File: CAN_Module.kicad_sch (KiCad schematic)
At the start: 14 parts, among them U3 SN65HVD231

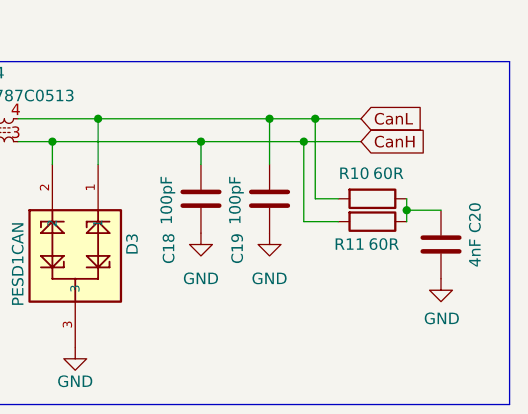
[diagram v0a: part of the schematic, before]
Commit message: added psu and formated board outline
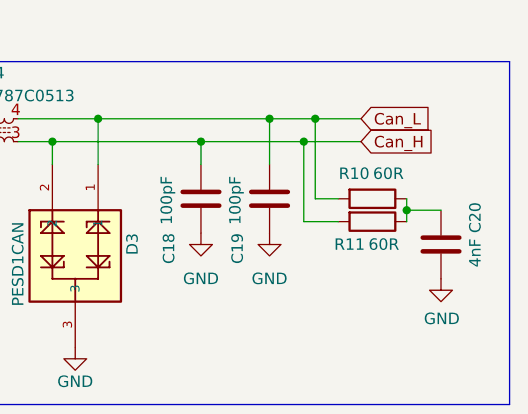
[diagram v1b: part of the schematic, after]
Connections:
- net CanH renamed Can_H
- net CanL renamed Can_L
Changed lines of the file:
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@@
 		)
 	)
-	(global_label "CanH"
+	(global_label "Can_H"
 		(shape input)
 		(at 144.78 26.67 0)
@@
 		)
 		(property "Intersheetrefs" "${INTERSHEET_REFS}"
-			(at 152.6637 26.67 0)
+			(at 153.6313 26.67 0)
 			(effects
 				(font
@@
 		)
 	)
-	(global_label "CanL"
+	(global_label "Can_L"
 		(shape input)
 		(at 144.78 24.13 0)
@@
 		)
 		(property "Intersheetrefs" "${INTERSHEET_REFS}"
-			(at 152.3613 24.13 0)
+			(at 153.3289 24.13 0)
 			(effects
 				(font

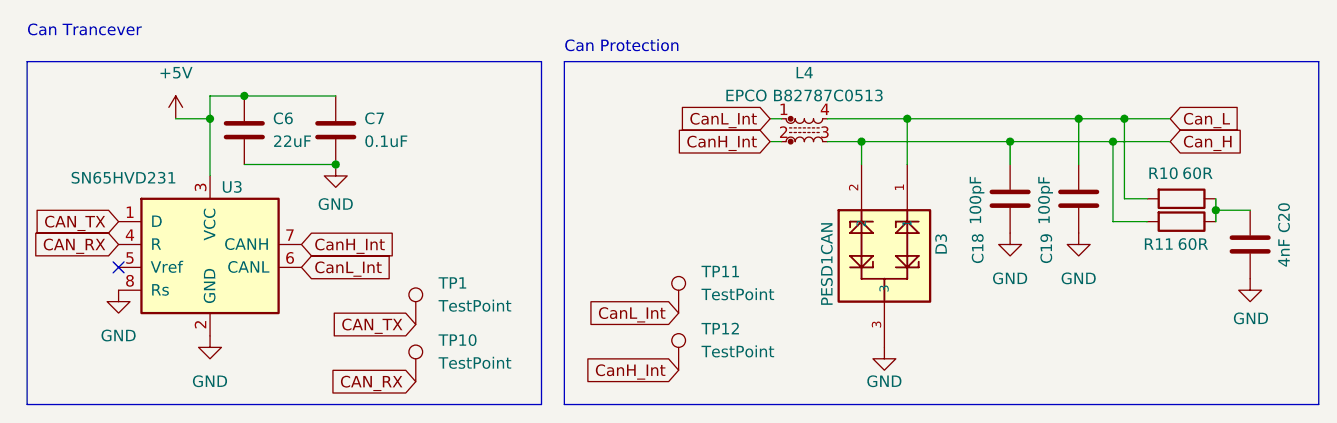
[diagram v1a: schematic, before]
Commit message: added footprint for a7670e
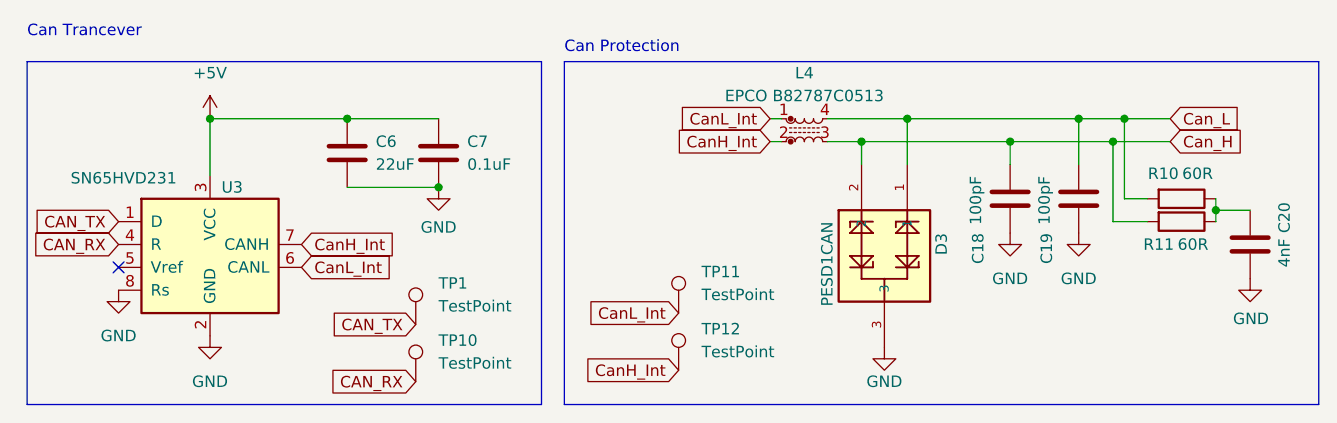
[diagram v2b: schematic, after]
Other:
- moved on the sheet: C6, C7
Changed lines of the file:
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@@
+	)
+	(junction
+		(at 134.62 24.13)
+		(diameter 0)
+		(color 0 0 0 0)
+	)
+	(junction
+		(at 127 26.67)
+		(diameter 0)
+		(color 0 0 0 0)
+	)
+	(junction
+		(at 115.57 24.13)
+		(diameter 0)
+		(color 0 0 0 0)
+	)
+	(junction
+		(at 149.86 34.29)
+		(diameter 0)
+		(color 0 0 0 0)
+	)
+	(junction
+		(at 110.49 26.67)
+		(diameter 0)
+		(color 0 0 0 0)
+	)
+	(junction
+		(at 138.43 26.67)
+		(diameter 0)
+		(color 0 0 0 0)
+	)
+	(junction
+		(at 53.34 24.13)
+		(diameter 0)
+		(color 0 0 0 0)
+	)
+	(junction
+		(at 63.5 31.75)
+		(diameter 0)
+		(color 0 0 0 0)
 	)
 	(junction
@@
 		(color 0 0 0 0)
 	)
-	(junction
-		(at 134.62 24.13)
-		(diameter 0)
-		(color 0 0 0 0)
-	)
-	(junction
-		(at 127 26.67)
-		(diameter 0)
-		(color 0 0 0 0)
-	)
-	(junction
-		(at 115.57 24.13)
-		(diameter 0)
-		(color 0 0 0 0)
-	)
-	(junction
-		(at 149.86 34.29)
-		(diameter 0)
-		(color 0 0 0 0)
-	)
-	(junction
-		(at 41.91 21.59)
-		(diameter 0)
-		(color 0 0 0 0)
-	)
-	(junction
-		(at 110.49 26.67)
-		(diameter 0)
-		(color 0 0 0 0)
-	)
-	(junction
-		(at 138.43 26.67)
-		(diameter 0)
-		(color 0 0 0 0)
-	)
-	(junction
-		(at 52.07 29.21)
-		(diameter 0)
-		(color 0 0 0 0)
-	)
 	(no_connect
 		(at 27.94 40.64)
@@
 	(wire
 		(pts
+			(xy 38.1 24.13) (xy 53.34 24.13)
+		)
+		(stroke
+			(width 0)
+			(type default)
+		)
+	)
+	(wire
+		(pts
 			(xy 138.43 26.67) (xy 138.43 35.56)
 		)
@@
 	(wire
 		(pts
-			(xy 38.1 24.13) (xy 38.1 21.59)
-		)
-		(stroke
-			(width 0)
-			(type default)
-		)
-	)
-	(wire
-		(pts
 			(xy 100.33 26.67) (xy 101.6 26.67)
 		)
@@
 	(wire
 		(pts
-			(xy 41.91 21.59) (xy 52.07 21.59)
+			(xy 53.34 24.13) (xy 63.5 24.13)
 		)
 		(stroke
@@
 	(wire
 		(pts
-			(xy 34.29 24.13) (xy 38.1 24.13)
-		)
-		(stroke
-			(width 0)
-			(type default)
-		)
-	)
-	(wire
-		(pts
 			(xy 115.57 24.13) (xy 115.57 29.21)
 		)
@@
 	(wire
 		(pts
-			(xy 38.1 21.59) (xy 41.91 21.59)
-		)
-		(stroke
-			(width 0)
-			(type default)
-		)
-	)
-	(wire
-		(pts
 			(xy 115.57 24.13) (xy 134.62 24.13)
 		)
@@
 	(wire
 		(pts
-			(xy 52.07 29.21) (xy 41.91 29.21)
+			(xy 63.5 31.75) (xy 53.34 31.75)
 		)
 		(stroke
@@
 	(symbol
 		(lib_id "power:+5V")
-		(at 34.29 24.13 0)
+		(at 38.1 24.13 0)
 		(mirror y)
 		(unit 1)
@@
 		(fields_autoplaced yes)
 		(property "Reference" "#PWR014"
-			(at 34.29 27.94 0)
+			(at 38.1 27.94 0)
 			(effects
 				(font
@@
 		)
 		(property "Value" "+5V"
-			(at 34.29 19.05 0)
+			(at 38.1 19.05 0)
 			(effects
 				(font
@@
 		)
 		(property "Footprint" ""
-			(at 34.29 24.13 0)
+			(at 38.1 24.13 0)
 			(effects
 				(font
@@
 		)
 		(property "Datasheet" ""
-			(at 34.29 24.13 0)
+			(at 38.1 24.13 0)
 			(effects
 				(font
@@
 		)
 		(property "Description" ""
-			(at 34.29 24.13 0)
+			(at 38.1 24.13 0)
 			(effects
 				(font
@@
 	(symbol
 		(lib_id "power:GND")
-		(at 52.07 29.21 0)
+		(at 63.5 31.75 0)
 		(unit 1)
 		(exclude_from_sim no)
@@
 		(fields_autoplaced yes)
 		(property "Reference" "#PWR016"
-			(at 52.07 35.56 0)
+			(at 63.5 38.1 0)
 			(effects
 				(font
@@
 		)
 		(property "Value" "GND"
-			(at 52.07 33.655 0)
+			(at 63.5 36.195 0)
 			(effects
 				(font
@@
 		)
 		(property "Footprint" ""
-			(at 52.07 29.21 0)
+			(at 63.5 31.75 0)
 			(effects
 				(font
@@
 		)
 		(property "Datasheet" ""
-			(at 52.07 29.21 0)
+			(at 63.5 31.75 0)
 			(effects
 				(font
@@
 		)
 		(property "Description" ""
-			(at 52.07 29.21 0)
+			(at 63.5 31.75 0)
 			(effects
 				(font
@@
 	(symbol
 		(lib_id "Device:C")
-		(at 41.91 25.4 0)
+		(at 53.34 27.94 0)
 		(unit 1)
 		(exclude_from_sim no)
@@
 		(fields_autoplaced yes)
 		(property "Reference" "C6"
-			(at 45.085 24.13 0)
+			(at 56.515 26.67 0)
 			(effects
 				(font
@@
 		)
 		(property "Value" "22uF"
-			(at 45.085 26.67 0)
+			(at 56.515 29.21 0)
 			(effects
 				(font
@@
 		)
 		(property "Footprint" "Capacitor_SMD:C_1206_3216Metric_Pad1.33x1.80mm_HandSolder"
-			(at 42.8752 29.21 0)
+			(at 54.3052 31.75 0)
 			(effects
 				(font
@@
 		)
 		(property "Datasheet" "~"
-			(at 41.91 25.4 0)
+			(at 53.34 27.94 0)
 			(effects
 				(font
@@
 		)
 		(property "Description" ""
-			(at 41.91 25.4 0)
+			(at 53.34 27.94 0)
 			(effects
 				(font
@@
 	(symbol
 		(lib_id "Device:C")
-		(at 52.07 25.4 0)
+		(at 63.5 27.94 0)
 		(unit 1)
 		(exclude_from_sim no)
@@
 		(fields_autoplaced yes)
 		(property "Reference" "C7"
-			(at 55.245 24.13 0)
+			(at 66.675 26.67 0)
 			(effects
 				(font
@@
 		)
 		(property "Value" "0.1uF"
-			(at 55.245 26.67 0)
+			(at 66.675 29.21 0)
 			(effects
 				(font
@@
 		)
 		(property "Footprint" "Capacitor_SMD:C_0805_2012Metric_Pad1.18x1.45mm_HandSolder"
-			(at 53.0352 29.21 0)
+			(at 64.4652 31.75 0)
 			(effects
 				(font
@@
 		)
 		(property "Datasheet" "~"
-			(at 52.07 25.4 0)
+			(at 63.5 27.94 0)
 			(effects
 				(font
@@
 		)
 		(property "Description" ""
-			(at 52.07 25.4 0)
-			(effects
-				(font
+			(at 63.5 27.94 0)
+			(effects
+				(font

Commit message: done most of the schematics
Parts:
- removed TP11, TP12: TestPoint, symbol Connector:TestPoint
- added TP4, TP5: TestPoint, symbol Connector:TestPoint
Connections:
- net CanH_Int renamed CANH
- net CANH: now also TP5.1
- net CanL_Int renamed CANL
- net CANL: now also TP4.1
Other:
- moved on the sheet: C6, C7, U3

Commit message: done refacoring
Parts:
- C18, C19: footprint Capacitor_SMD:C_0805_2012Metric_Pad1.18x1.45mm_HandSolder -> (none)
- TP1, TP10, TP4, TP5: footprint (none) -> TestPoint:TestPoint_Pad_D2.5mm
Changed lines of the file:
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@@
 			)
 		)
-		(property "Footprint" ""
+		(property "Footprint" "TestPoint:TestPoint_Pad_D2.5mm"
 			(at 95.25 41.91 0)
 			(effects
@@
 			)
 		)
-		(property "Footprint" "Capacitor_SMD:C_0805_2012Metric_Pad1.18x1.45mm_HandSolder"
+		(property "Footprint" ""
 			(at 133.6548 29.21 0)
 			(effects
@@
 			)
 		)
-		(property "Footprint" ""
+		(property "Footprint" "TestPoint:TestPoint_Pad_D2.5mm"
 			(at 66.04 46.99 0)
 			(effects
@@
 			)
 		)
-		(property "Footprint" ""
+		(property "Footprint" "TestPoint:TestPoint_Pad_D2.5mm"
 			(at 95.25 48.26 0)
 			(effects
@@
 			)
 		)
-		(property "Footprint" ""
+		(property "Footprint" "TestPoint:TestPoint_Pad_D2.5mm"
 			(at 66.04 53.34 0)
 			(effects
@@
 			)
 		)
-		(property "Footprint" "Capacitor_SMD:C_0805_2012Metric_Pad1.18x1.45mm_HandSolder"
+		(property "Footprint" ""
 			(at 126.0348 29.21 0)
 			(effects

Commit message: assigned most footprints
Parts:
- C6: footprint Capacitor_SMD:C_1206_3216Metric_Pad1.33x1.80mm_HandSolder -> (none)
- C7: footprint Capacitor_SMD:C_0805_2012Metric_Pad1.18x1.45mm_HandSolder -> (none)
- R10, R11: footprint Resistor_SMD:R_1206_3216Metric_Pad1.30x1.75mm_HandSolder -> Resistor_SMD:R_0603_1608Metric
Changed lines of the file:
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@@
 			)
 		)
-		(property "Footprint" "Resistor_SMD:R_1206_3216Metric_Pad1.30x1.75mm_HandSolder"
+		(property "Footprint" "Resistor_SMD:R_0603_1608Metric"
 			(at 146.05 31.242 90)
 			(effects
@@
 			)
 		)
-		(property "Footprint" "Capacitor_SMD:C_1206_3216Metric_Pad1.33x1.80mm_HandSolder"
+		(property "Footprint" ""
 			(at 55.5752 33.02 0)
 			(effects
@@
 			)
 		)
-		(property "Footprint" "Resistor_SMD:R_1206_3216Metric_Pad1.30x1.75mm_HandSolder"
+		(property "Footprint" "Resistor_SMD:R_0603_1608Metric"
 			(at 146.05 33.782 90)
 			(effects
@@
 			)
 		)
-		(property "Footprint" "Capacitor_SMD:C_0805_2012Metric_Pad1.18x1.45mm_HandSolder"
+		(property "Footprint" ""
 			(at 65.7352 33.02 0)
 			(effects

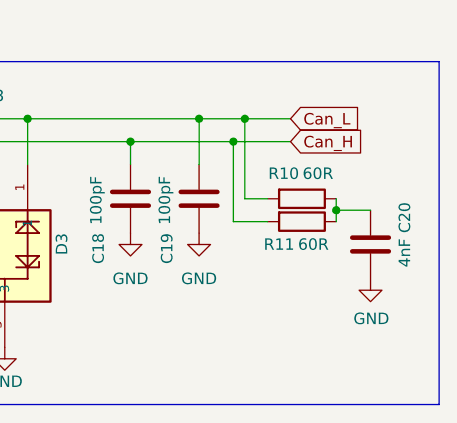
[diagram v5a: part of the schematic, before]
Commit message: cleaned up scematics and updated power management
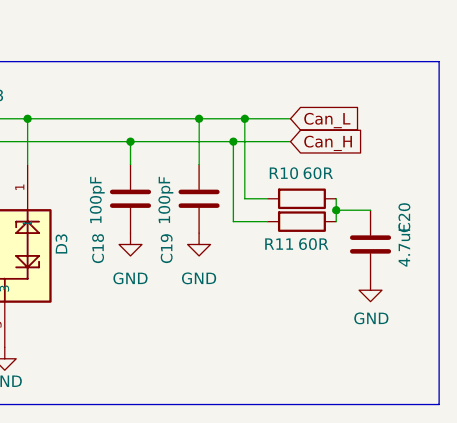
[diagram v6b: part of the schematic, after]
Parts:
- C18, C19, C7: footprint (none) -> Capacitor_SMD:C_0805_2012Metric
- C20: value 4nF -> 4.7uF; footprint Capacitor_SMD:C_0805_2012Metric_Pad1.18x1.45mm_HandSolder -> Capacitor_SMD:C_0805_2012Metric
- C6: footprint (none) -> Capacitor_SMD:C_0603_1608Metric

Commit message: finelized scematics
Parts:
- L4: footprint footprints:EPCO B82787C0513 -> EPCO_B82787C0513:EPCO B82787C0513
- TP1, TP10, TP4, TP5: footprint TestPoint:TestPoint_Pad_D2.5mm -> TestPoint:TestPoint_Pad_D2.0mm
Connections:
- net Can_H renamed CAN_H
- net Can_L renamed CAN_L
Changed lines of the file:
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@@
+		)
+	)
+	(global_label "CAN_L"
+		(shape input)
+		(at 144.78 24.13 0)
+		(fields_autoplaced yes)
+		(effects
+			(font
+				(size 1.27 1.27)
+			)
+			(justify left)
+		)
+		(property "Intersheetrefs" "${INTERSHEET_REFS}"
+			(at 153.45 24.13 0)
+			(effects
+				(font
+					(size 1.27 1.27)
+				)
+				(justify left)
+				(hide yes)
+			)
 		)
 	)
@@
 		)
 	)
-	(global_label "Can_H"
-		(shape input)
-		(at 144.78 26.67 0)
-		(fields_autoplaced yes)
-		(effects
-			(font
-				(size 1.27 1.27)
-			)
-			(justify left)
-		)
-		(property "Intersheetrefs" "${INTERSHEET_REFS}"
-			(at 153.6313 26.67 0)
-			(effects
-				(font
-					(size 1.27 1.27)
-				)
-				(justify left)
-				(hide yes)
-			)
-		)
-	)
 	(global_label "CAN_RX"
 		(shape input)
@@
 				)
 				(justify right)
+				(hide yes)
+			)
+		)
+	)
+	(global_label "CAN_H"
+		(shape input)
+		(at 144.78 26.67 0)
+		(fields_autoplaced yes)
+		(effects
+			(font
+				(size 1.27 1.27)
+			)
+			(justify left)
+		)
+		(property "Intersheetrefs" "${INTERSHEET_REFS}"
+			(at 153.7524 26.67 0)
+			(effects
+				(font
+					(size 1.27 1.27)
+				)
+				(justify left)
 				(hide yes)
 			)
@@
 				)
 				(justify right)
-				(hide yes)
-			)
-		)
-	)
-	(global_label "Can_L"
-		(shape input)
-		(at 144.78 24.13 0)
-		(fields_autoplaced yes)
-		(effects
-			(font
-				(size 1.27 1.27)
-			)
-			(justify left)
-		)
-		(property "Intersheetrefs" "${INTERSHEET_REFS}"
-			(at 153.3289 24.13 0)
-			(effects
-				(font
-					(size 1.27 1.27)
-				)
-				(justify left)
 				(hide yes)
 			)
@@
 			)
 		)
-		(property "Footprint" "TestPoint:TestPoint_Pad_D2.5mm"
+		(property "Footprint" "TestPoint:TestPoint_Pad_D2.0mm"
 			(at 95.25 41.91 0)
 			(effects
@@
 			)
 		)
-		(property "Footprint" "TestPoint:TestPoint_Pad_D2.5mm"
+		(property "Footprint" "TestPoint:TestPoint_Pad_D2.0mm"
 			(at 66.04 46.99 0)
 			(effects
@@
 			)
 		)
-		(property "Footprint" "footprints:EPCO B82787C0513"
+		(property "Footprint" "EPCO_B82787C0513:EPCO B82787C0513"
 			(at 104.14 25.4 0)
 			(effects
@@
 			)
 		)
-		(property "Footprint" "TestPoint:TestPoint_Pad_D2.5mm"
+		(property "Footprint" "TestPoint:TestPoint_Pad_D2.0mm"
 			(at 95.25 48.26 0)
 			(effects
@@
 			)
 		)
-		(property "Footprint" "TestPoint:TestPoint_Pad_D2.5mm"
+		(property "Footprint" "TestPoint:TestPoint_Pad_D2.0mm"
 			(at 66.04 53.34 0)
 			(effects

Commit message: mostly layouted
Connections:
- net CANH: now also L4.1; no longer L4.2
- net CANL: now also L4.2; no longer L4.1
- net CAN_H: now also C19.2, D3.1, L4.4, R10.2; no longer C18.2, D3.2, L4.3, R11.2
- net CAN_L: now also C18.2, D3.2, L4.3, R11.2; no longer C19.2, D3.1, L4.4, R10.2
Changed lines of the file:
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@@
+	)
+	(junction
+		(at 134.62 24.13)
+		(diameter 0)
+		(color 0 0 0 0)
+	)
+	(junction
+		(at 54.61 25.4)
+		(diameter 0)
+		(color 0 0 0 0)
+	)
+	(junction
+		(at 127 26.67)
+		(diameter 0)
+		(color 0 0 0 0)
+	)
+	(junction
+		(at 115.57 24.13)
+		(diameter 0)
+		(color 0 0 0 0)
+	)
+	(junction
+		(at 138.43 26.67)
+		(diameter 0)
+		(color 0 0 0 0)
+	)
+	(junction
+		(at 149.86 34.29)
+		(diameter 0)
+		(color 0 0 0 0)
+	)
+	(junction
+		(at 110.49 26.67)
+		(diameter 0)
+		(color 0 0 0 0)
 	)
 	(junction
 		(at 139.7 24.13)
-		(diameter 0)
-		(color 0 0 0 0)
-	)
-	(junction
-		(at 134.62 24.13)
-		(diameter 0)
-		(color 0 0 0 0)
-	)
-	(junction
-		(at 54.61 25.4)
-		(diameter 0)
-		(color 0 0 0 0)
-	)
-	(junction
-		(at 127 26.67)
-		(diameter 0)
-		(color 0 0 0 0)
-	)
-	(junction
-		(at 115.57 24.13)
-		(diameter 0)
-		(color 0 0 0 0)
-	)
-	(junction
-		(at 149.86 34.29)
-		(diameter 0)
-		(color 0 0 0 0)
-	)
-	(junction
-		(at 110.49 26.67)
-		(diameter 0)
-		(color 0 0 0 0)
-	)
-	(junction
-		(at 138.43 26.67)
 		(diameter 0)
 		(color 0 0 0 0)
@@
 		)
 	)
+	(wire
+		(pts
+			(xy 100.33 24.13) (xy 101.6 24.13)
+		)
+		(stroke
+			(width 0)
+			(type default)
+		)
+	)
 	(polyline
 		(pts
@@
 	(wire
 		(pts
-			(xy 100.33 24.13) (xy 101.6 24.13)
+			(xy 100.33 26.67) (xy 101.6 26.67)
 		)
 		(stroke
@@
 	(wire
 		(pts
+			(xy 138.43 26.67) (xy 142.24 26.67)
+		)
+		(stroke
+			(width 0)
+			(type default)
+		)
+	)
+	(wire
+		(pts
 			(xy 134.62 24.13) (xy 139.7 24.13)
 		)
@@
 	(wire
 		(pts
-			(xy 100.33 26.67) (xy 101.6 26.67)
-		)
-		(stroke
-			(width 0)
-			(type default)
-		)
-	)
-	(wire
-		(pts
 			(xy 40.64 25.4) (xy 54.61 25.4)
 		)
@@
 	(wire
 		(pts
-			(xy 139.7 24.13) (xy 144.78 24.13)
-		)
-		(stroke
-			(width 0)
-			(type default)
-		)
-	)
-	(wire
-		(pts
 			(xy 54.61 25.4) (xy 64.77 25.4)
 		)
@@
 	(wire
 		(pts
-			(xy 138.43 26.67) (xy 144.78 26.67)
-		)
-		(stroke
-			(width 0)
-			(type default)
-		)
-	)
-	(wire
-		(pts
 			(xy 149.86 33.02) (xy 149.86 34.29)
 		)
@@
 		(pts
 			(xy 64.77 33.02) (xy 54.61 33.02)
+		)
+		(stroke
+			(width 0)
+			(type default)
+		)
+	)
+	(wire
+		(pts
+			(xy 139.7 24.13) (xy 142.24 24.13)
 		)
 		(stroke
@@
 	)
 	(label "CANL"
+		(at 100.33 26.67 180)
+		(fields_autoplaced yes)
+		(effects
+			(font
+				(size 1.27 1.27)
+			)
+			(justify right bottom)
+		)
+	)
+	(label "CANH"
 		(at 100.33 24.13 180)
-		(fields_autoplaced yes)
-		(effects
-			(font
-				(size 1.27 1.27)
-			)
-			(justify right bottom)
-		)
-	)
-	(label "CANH"
-		(at 100.33 26.67 180)
 		(fields_autoplaced yes)
 		(effects
@@
 	(global_label "CAN_L"
 		(shape input)
-		(at 144.78 24.13 0)
+		(at 142.24 26.67 0)
 		(fields_autoplaced yes)
 		(effects
@@
 		)
 		(property "Intersheetrefs" "${INTERSHEET_REFS}"
-			(at 153.45 24.13 0)
+			(at 150.91 26.67 0)
 			(effects
 				(font
@@
 	(global_label "CAN_H"
 		(shape input)
-		(at 144.78 26.67 0)
+		(at 142.24 24.13 0)
 		(fields_autoplaced yes)
 		(effects
@@
 		)
 		(property "Intersheetrefs" "${INTERSHEET_REFS}"
-			(at 153.7524 26.67 0)
+			(at 151.2124 24.13 0)
 			(effects
 				(font
